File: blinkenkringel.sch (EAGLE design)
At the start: 88 parts, among them Q1 IRLML2502, Q2 BC337-40, Q3 BC337-40, Q4 BC337-40, Q5 BC337-40

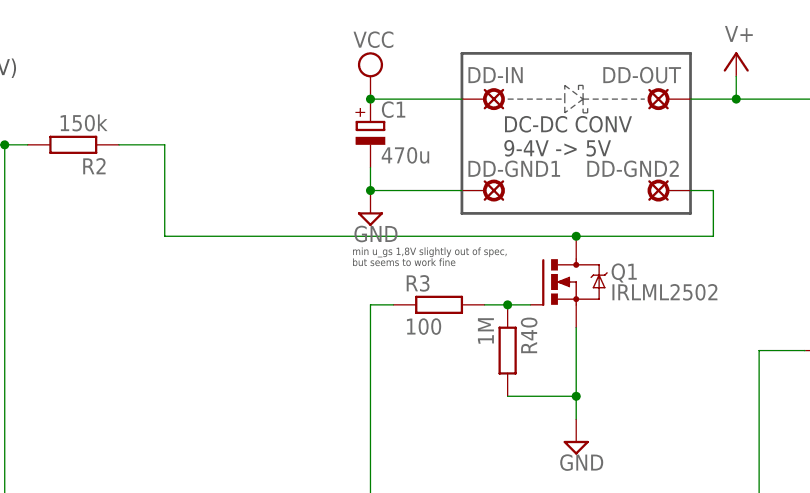
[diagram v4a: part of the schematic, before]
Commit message: got the cap connected wrong
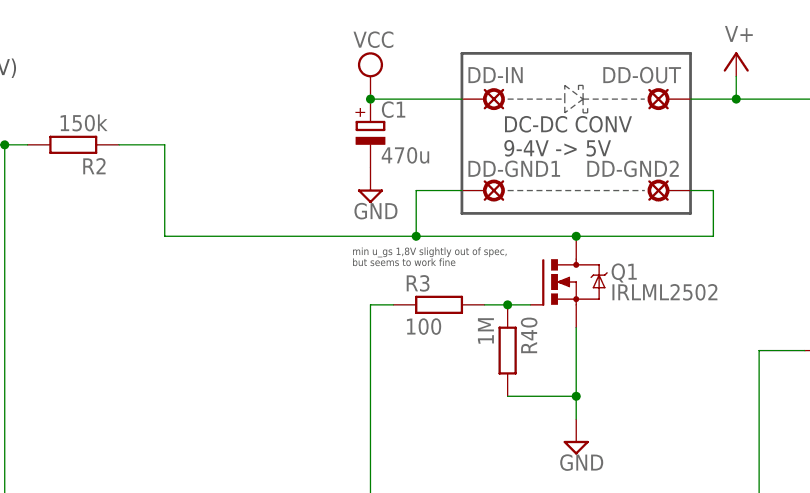
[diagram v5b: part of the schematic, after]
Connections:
- net GND: no longer DD-GND1.MP
- net N$5: now also DD-GND1.MP
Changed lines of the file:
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@@
 <text x="7.62" y="71.12" size="1.778" layer="97">grün</text>
 <text x="7.62" y="63.5" size="1.778" layer="97">rot</text>
+<wire x1="134.62" y1="154.94" x2="149.86" y2="154.94" width="0.1" layer="97" style="shortdash"/>
 </plain>
 <instances>
@@
 <instance part="R40" gate="G$1" x="134.62" y="137.16" rot="R270"/>
 <instance part="R41" gate="1" x="43.18" y="160.02" rot="R270"/>
-<instance part="SUPPLY16" gate="GND" x="119.38" y="152.4"/>
+<instance part="SUPPLY16" gate="GND" x="119.38" y="154.94"/>
 </instances>
 <busses>
@@
 <wire x1="91.44" y1="160.02" x2="96.52" y2="160.02" width="0.1524" layer="91"/>
 <wire x1="96.52" y1="160.02" x2="96.52" y2="149.86" width="0.1524" layer="91"/>
-<wire x1="96.52" y1="149.86" x2="142.24" y2="149.86" width="0.1524" layer="91"/>
+<wire x1="96.52" y1="149.86" x2="124.46" y2="149.86" width="0.1524" layer="91"/>
 <pinref part="Q1" gate="G$1" pin="D"/>
 <junction x="142.24" y="149.86"/>
+<pinref part="DD-GND1" gate="1" pin="MP"/>
+<wire x1="124.46" y1="149.86" x2="142.24" y2="149.86" width="0.1524" layer="91"/>
+<wire x1="129.54" y1="154.94" x2="124.46" y2="154.94" width="0.1524" layer="91"/>
+<wire x1="124.46" y1="154.94" x2="124.46" y2="149.86" width="0.1524" layer="91"/>
+<junction x="124.46" y="149.86"/>
 </segment>
 </net>
@@
 <segment>
 <pinref part="C1" gate="G$1" pin="-"/>
-<pinref part="DD-GND1" gate="1" pin="MP"/>
-<wire x1="129.54" y1="154.94" x2="119.38" y2="154.94" width="0.1524" layer="91"/>
-<wire x1="119.38" y1="154.94" x2="119.38" y2="157.48" width="0.1524" layer="91"/>
 <pinref part="SUPPLY16" gate="GND" pin="GND"/>
-<junction x="119.38" y="154.94"/>
-</segment>
-</net>
+</segment>
+</net>
